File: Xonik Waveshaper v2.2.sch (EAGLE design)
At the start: 98 parts, among them IC1 TL074JT, IC2 TL074JT, IC3 TL074JT, IC4 TL072JT, IC5 4013T, IC6 LM311T, T1 2n3904

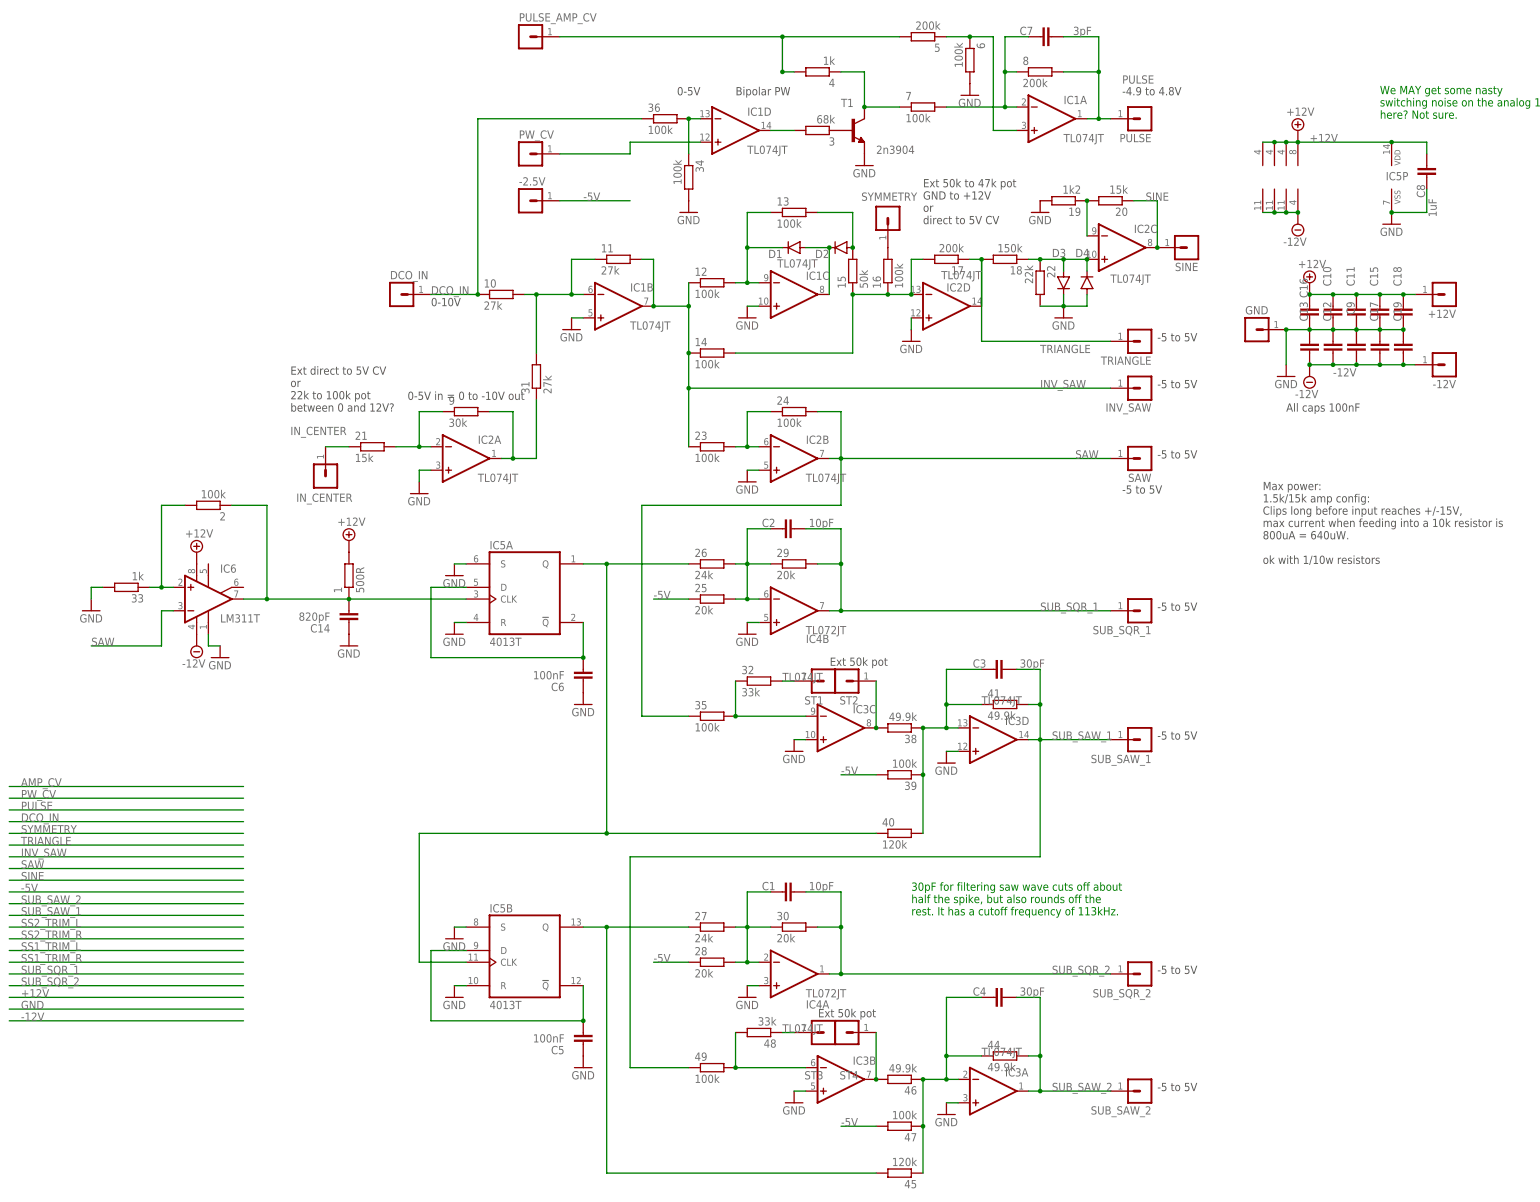
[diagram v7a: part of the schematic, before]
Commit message: Switched to single connector
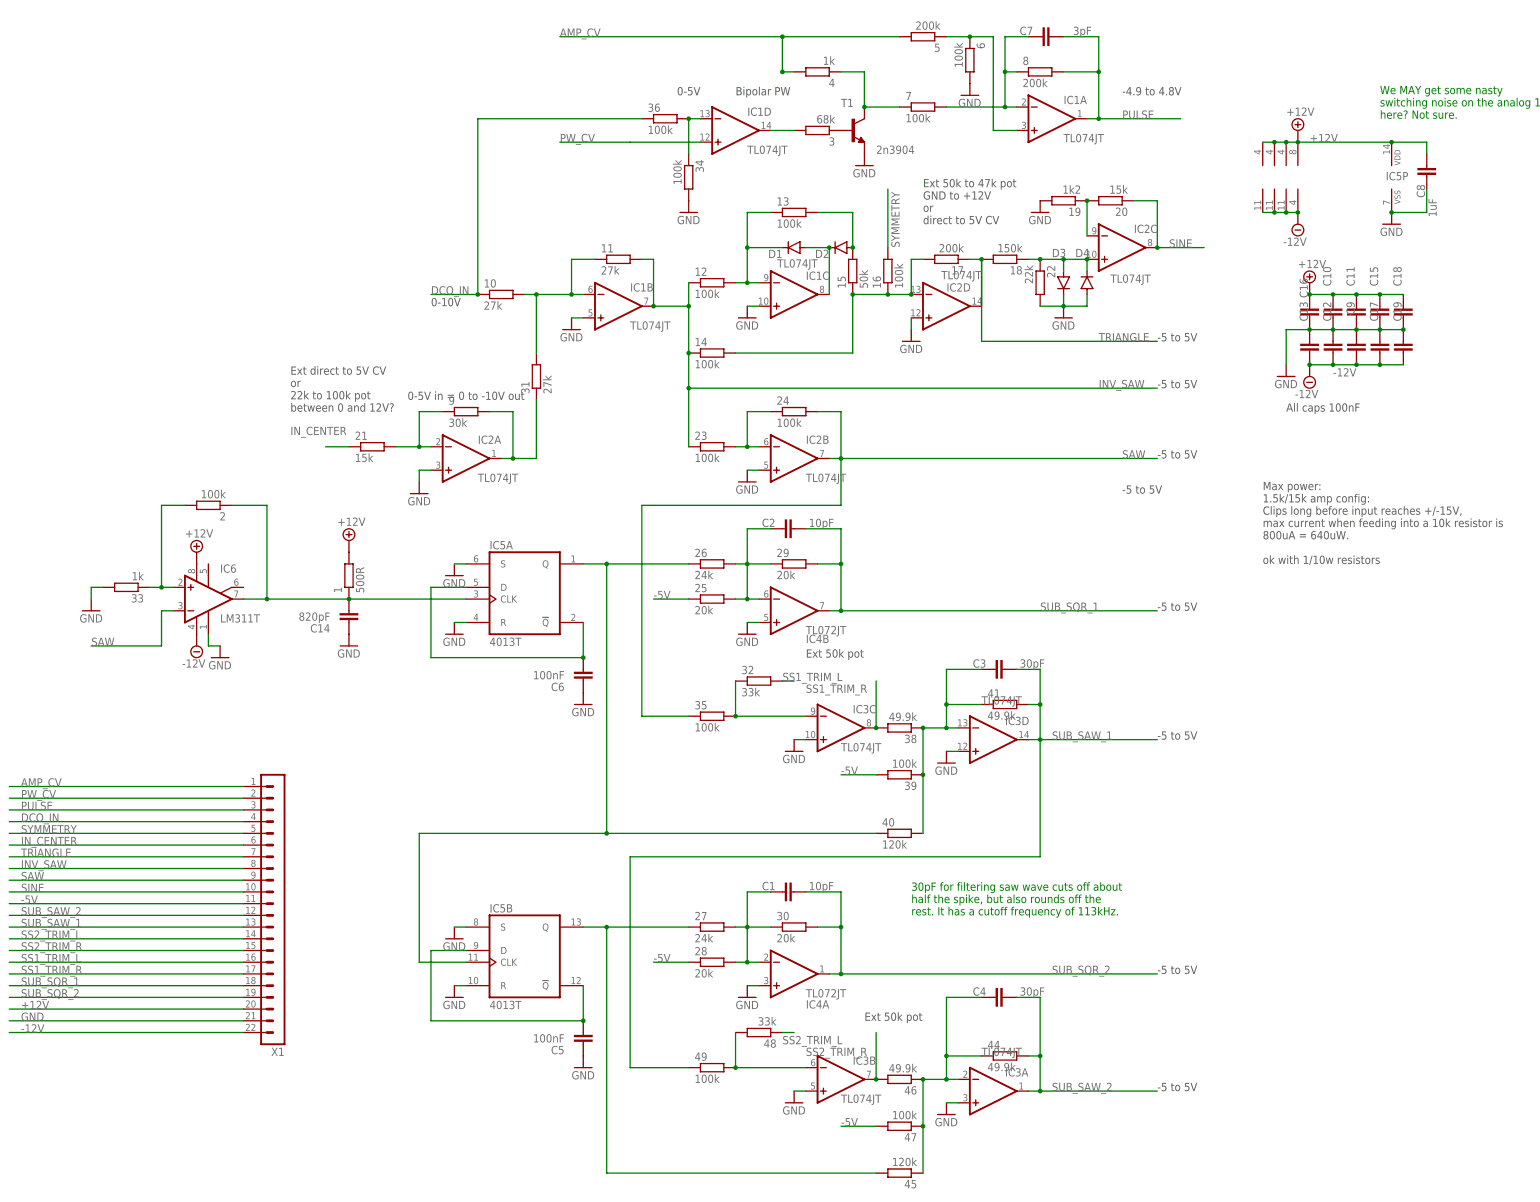
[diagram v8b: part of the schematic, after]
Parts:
- removed +12V, -12V, -2.5V, DCO_IN, GND, INV_SAW, IN_CENTER, PULSE, PULSE_AMP_CV, PW_CV, SAW, SINE, ST1, ST2, ST3, ST4, SUB_SAW_1, SUB_SAW_2, SUB_SQR_1, SUB_SQR_2, SYMMETRY, TRIANGLE: (no value), joakim:MA01-1JN
- added X1: (no value), joakim:MA22-1JN
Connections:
- net +12V: now also X1.20; no longer +12V.1
- net -12V: now also X1.22; no longer -12V.1
- net -5V: now also X1.11; no longer -2.5V.1
- net AMP_CV: now also X1.1; no longer PULSE_AMP_CV.1
- net DCO_IN: now also X1.4; no longer DCO_IN.1
- net GND: now also X1.21; no longer GND.1
- net INV_SAW: now also X1.8; no longer INV_SAW.1
- net IN_CENTER: now also X1.6; no longer IN_CENTER.1
- net PULSE: now also X1.3; no longer PULSE.1
- net PW_CV: now also X1.2; no longer PW_CV.1
- net SAW: now also X1.9; no longer SAW.1
- net SINE: now also X1.10; no longer SINE.1
- net SS1_TRIM_L: now also X1.16; no longer ST1.1
- net SS1_TRIM_R: now also X1.17; no longer ST2.1
- net SS2_TRIM_L: now also X1.14; no longer ST3.1
- net SS2_TRIM_R: now also X1.15; no longer ST4.1
- net SUB_SAW_1: now also X1.13; no longer SUB_SAW_1.1
- net SUB_SAW_2: now also X1.12; no longer SUB_SAW_2.1
- net SUB_SQR_1: now also X1.18; no longer SUB_SQR_1.1
- net SUB_SQR_2: now also X1.19; no longer SUB_SQR_2.1
- net SYMMETRY: now also X1.5; no longer SYMMETRY.1
- net TRIANGLE: now also X1.7; no longer TRIANGLE.1
